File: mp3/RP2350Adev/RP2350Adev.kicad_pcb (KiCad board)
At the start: 2 copper layers, 30.9 x 51.8 mm, 44 parts, among them J1 USB4105-GF-A, J2 LEFT, J4 RIGHT, U1 W25Q32JV, U2 RP2350A, U3 MCP1702T-3302E_CB, X1 IQXO-791

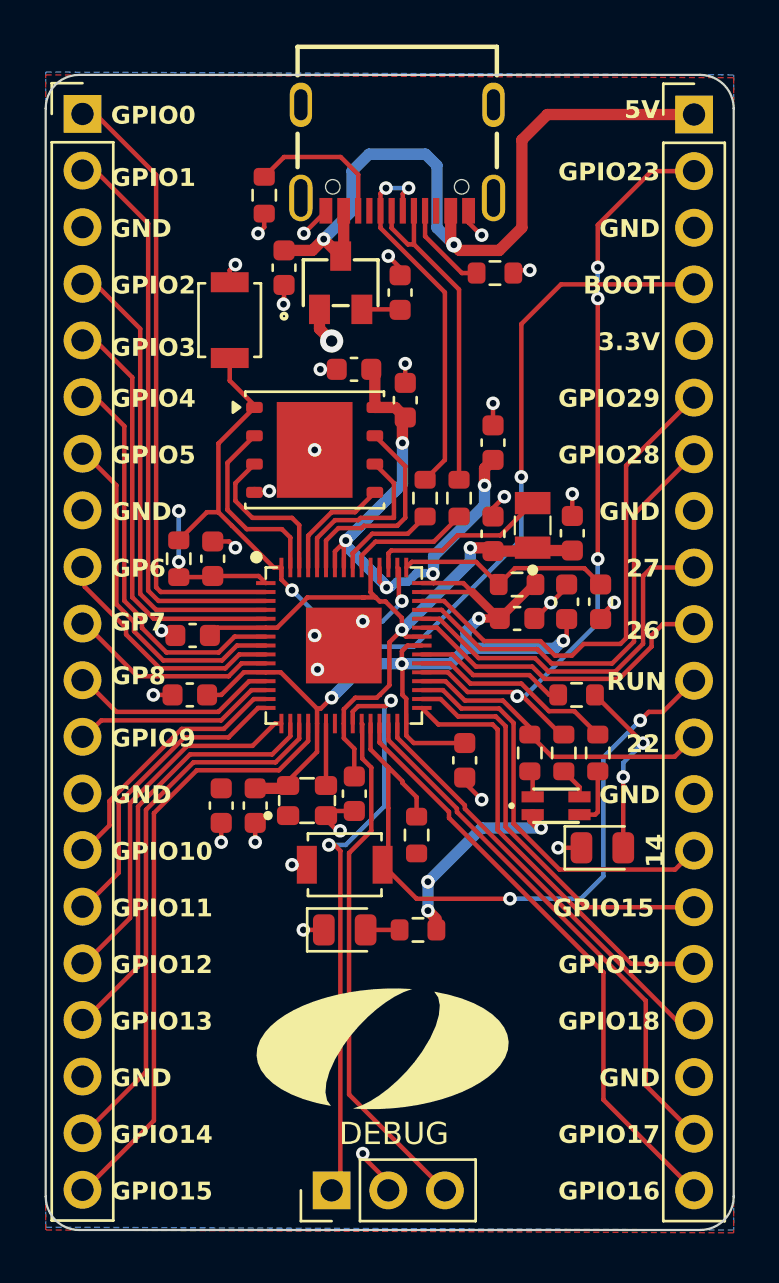
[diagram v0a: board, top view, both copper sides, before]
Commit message: Update board sizing to be 50x32mm
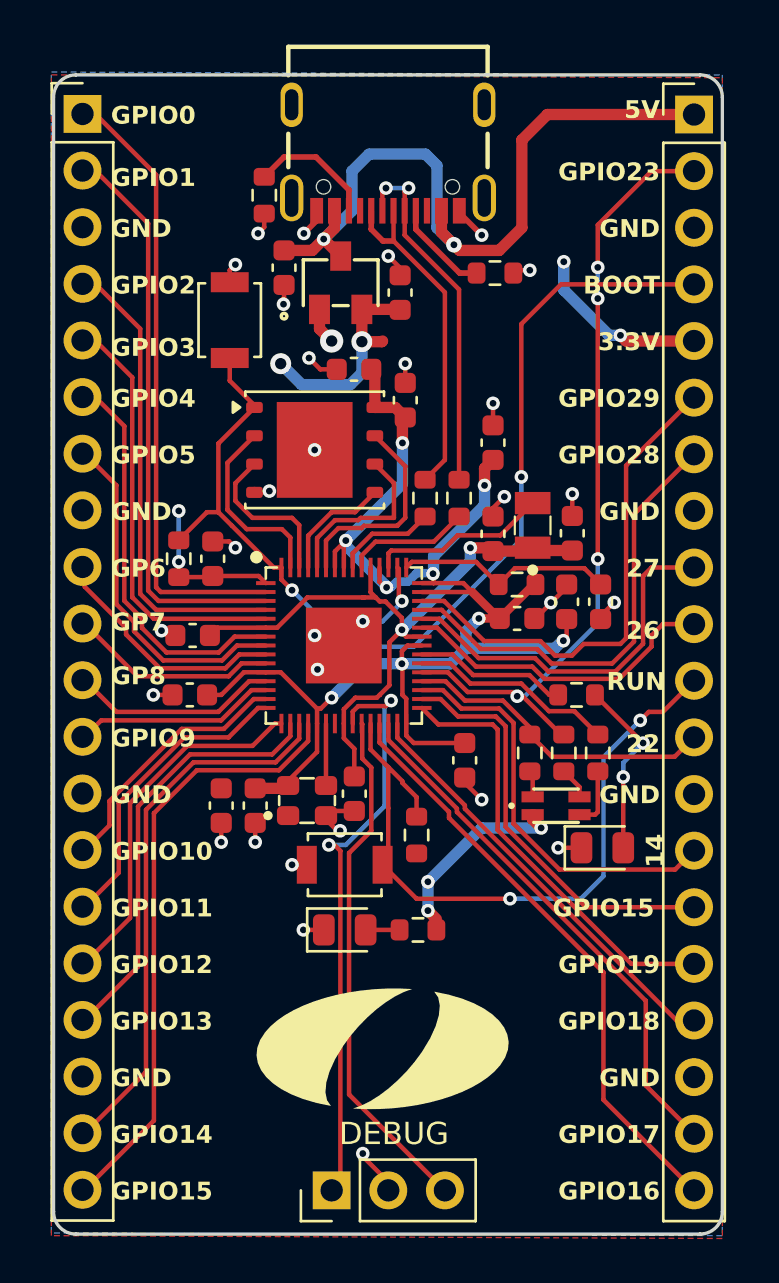
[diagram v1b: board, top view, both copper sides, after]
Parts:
- moved J1 0.41 mm to (42.7, 24.2)
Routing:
- net +3V3: track 87.6 -> 103.7 mm, vias 14 -> 18
- net Net-(J1-D+-PadA6): track 16.9 -> 15.4 mm, vias 2 -> 0
- net Net-(J1-D--PadA7): track 15.0 -> 16.3 mm, vias 0 -> 2
- net Net-(J1-CC1): track 4.14 -> 5.03 mm
- net Net-(J1-CC2): track 6.54 -> 5.72 mm
- net GND: track 42.6 -> 43.3 mm
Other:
- board size 30.9 x 51.8 mm -> 30 x 52 mm

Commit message: Add mounting holes
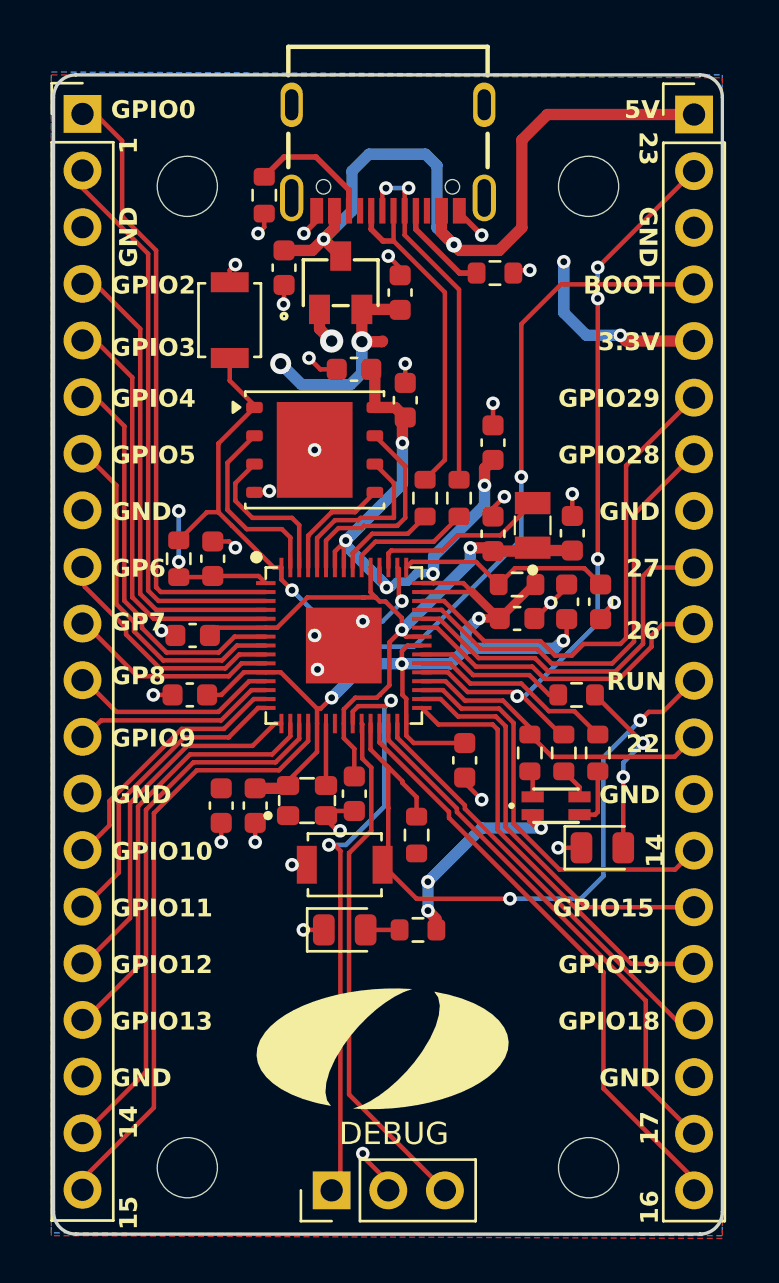
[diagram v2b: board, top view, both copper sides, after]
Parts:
- added REF**: MountingHole_2.7mm_M2.5_DIN965, MountingHole:MountingHole_2.7mm_M2.5_DIN965, F.Cu at (33.7, 27.9)
- added REF**: MountingHole_2.7mm_M2.5_DIN965, MountingHole:MountingHole_2.7mm_M2.5_DIN965, F.Cu at (51.7, 71.9)
- added REF**: MountingHole_2.7mm_M2.5_DIN965, MountingHole:MountingHole_2.7mm_M2.5_DIN965, F.Cu at (51.7, 27.9)
- added REF**: MountingHole_2.7mm_M2.5_DIN965, MountingHole:MountingHole_2.7mm_M2.5_DIN965, F.Cu at (33.7, 71.9)
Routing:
- net /GPIO23: track 35.9 -> 34.8 mm
- net +3V3: track 103.7 -> 104.3 mm
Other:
- board text added: "1"
- board text added: "15"
- board text added: "16"
- board text added: "17"
- board text added: "23"
- board text removed: "GPIO1"
- board text removed: "GPIO14"
- board text removed: "GPIO16"
- board text removed: "GPIO17"
- board text removed: "GPIO23"

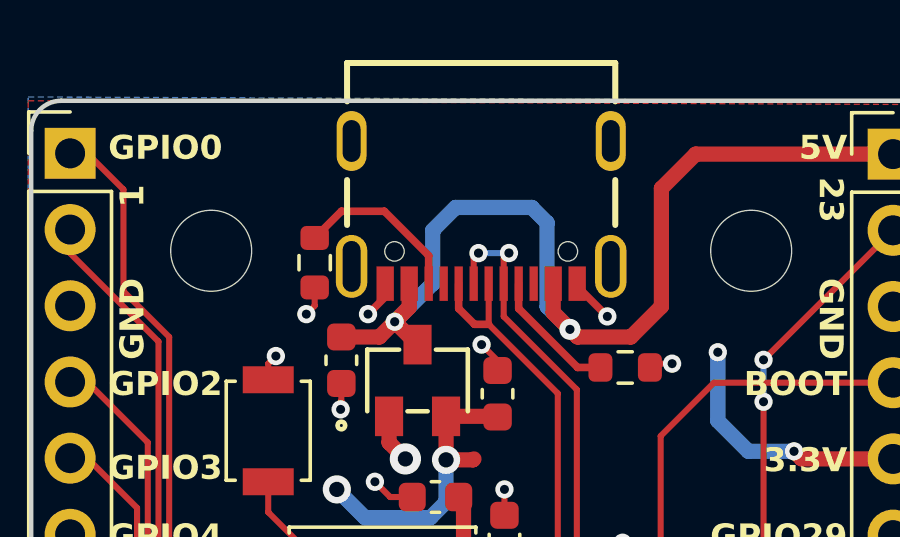
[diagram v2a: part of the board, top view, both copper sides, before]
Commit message: Update mounting holes for DRC
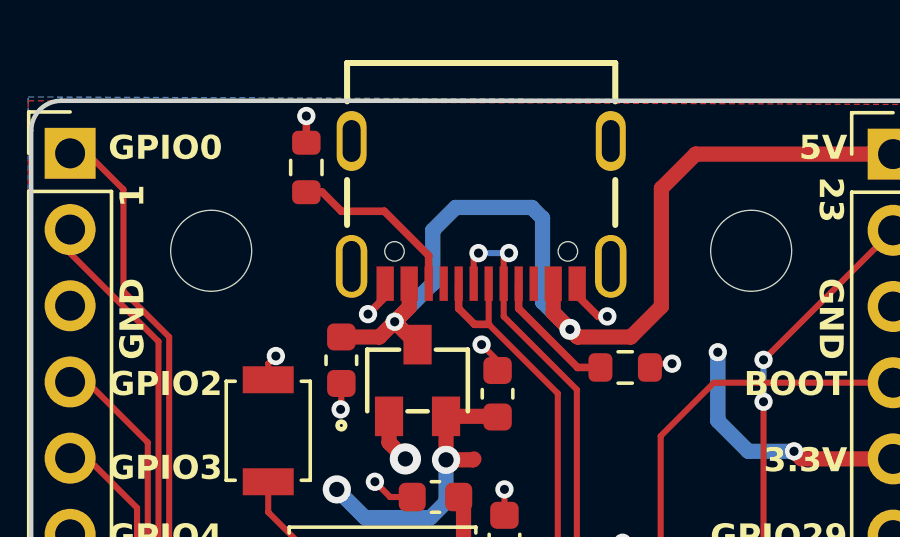
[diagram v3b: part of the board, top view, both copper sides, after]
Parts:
- moved R3 3.19 mm to (36.8, 25.1), turned to 90 degrees
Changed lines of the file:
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@@
 	(footprint "Resistor_SMD:R_0603_1608Metric"
 		(layer "F.Cu")
-		(at 37.108 28.258 -90)
+		(at 36.83 25.083 90)
 		(descr "Resistor SMD 0603 (1608 Metric), square (rectangular) end terminal, IPC-7351 nominal, (Body size source: IPC-SM-782 page 72, https://www.pcb-3d.com/wordpress/wp-content/uploads/ipc-sm-782a_amendment_1_and_2.pdf), generated with kicad-footprint-generator")
 		(tags "resistor")
@@
 		(attr smd)
 		(fp_line
-			(start -0.237258 0.5225)
-			(end 0.237258 0.5225)
+			(start -0.237258 -0.5225)
+			(end 0.237258 -0.5225)
 			(stroke
 				(width 0.12)
@@
 		)
 		(fp_line
-			(start -0.237258 -0.5225)
-			(end 0.237258 -0.5225)
+			(start -0.237258 0.5225)
+			(end 0.237258 0.5225)
 			(stroke
 				(width 0.12)
@@
 		)
 		(pad "1" smd roundrect
-			(at -0.825 0 270)
+			(at -0.825 0 90)
 			(size 0.8 0.95)
 			(layers "F.Cu" "F.Mask" "F.Paste")
@@
 		)
 		(pad "2" smd roundrect
-			(at 0.825 0 270)
+			(at 0.825 0 90)
 			(size 0.8 0.95)
 			(layers "F.Cu" "F.Mask" "F.Paste")
@@
 	)
 	(segment
+		(start 45.858 29.348)
+		(end 46.5582 30.0482)
+		(width 0.254)
+		(layer "F.Cu")
+		(net 2)
+	)
+	(segment
 		(start 39.878 56.087)
 		(end 39.544 56.087)
@@
 	)
 	(segment
+		(start 46.5582 30.0482)
+		(end 46.863 30.0482)
+		(width 0.254)
+		(layer "F.Cu")
+		(net 2)
+	)
+	(segment
 		(start 41.148 55.88)
 		(end 40.085 55.88)
@@
 	)
 	(segment
-		(start 36.83 29.972)
-		(end 37.108 29.694)
-		(width 0.2032)
-		(layer "F.Cu")
-		(net 2)
-	)
-	(segment
 		(start 46.101 54.382)
 		(end 46.101 54.61)
@@
 	)
 	(segment
-		(start 45.858 29.0432)
-		(end 46.863 30.0482)
-		(width 0.254)
-		(layer "F.Cu")
-		(net 2)
-	)
-	(segment
 		(start 41.529 71.247)
 		(end 41.529 71.374)
@@
 	)
 	(segment
+		(start 36.83 24.258)
+		(end 36.83 23.368)
+		(width 0.254)
+		(layer "F.Cu")
+		(net 2)
+	)
+	(segment
 		(start 40.678 48.458)
 		(end 39.822 48.458)
@@
 	)
 	(segment
+		(start 45.858 28.956)
+		(end 45.858 29.348)
+		(width 0.254)
+		(layer "F.Cu")
+		(net 2)
+	)
+	(segment
 		(start 47.371 42.291)
 		(end 47.879 41.783)
@@
 	)
 	(segment
-		(start 37.108 29.694)
-		(end 37.108 29.083)
-		(width 0.2032)
-		(layer "F.Cu")
-		(net 2)
-	)
-	(segment
 		(start 37.211 41.529)
 		(end 37.152 41.588)
@@
 	)
 	(segment
-		(start 45.858 28.956)
-		(end 45.858 29.0432)
-		(width 0.254)
-		(layer "F.Cu")
-		(net 2)
-	)
-	(segment
 		(start 49.276 47.244)
 		(end 49.2252 47.244)
@@
 	)
 	(via
-		(at 36.83 29.972)
-		(size 0.6096)
-		(drill 0.3)
-		(layers "F.Cu" "B.Cu")
-		(net 2)
-	)
-	(via
 		(at 40.132 34.798)
 		(size 1.0414)
@@
 	)
 	(via
+		(at 36.83 23.368)
+		(size 0.6096)
+		(drill 0.3048)
+		(layers "F.Cu" "B.Cu")
+		(net 2)
+	)
+	(via
 		(at 35.179 57.277)
 		(size 0.6096)
@@
 	)
 	(segment
-		(start 44.855 29.718)
+		(start 44.704 29.567)
 		(end 45.617 30.48)
 		(width 0.508)
@@
 	)
 	(segment
-		(start 39.775 30.226)
-		(end 41.045 28.956)
+		(start 44.704 26.773)
+		(end 44.704 29.567)
 		(width 0.508)
 		(layer "B.Cu")
@@
 	)
 	(segment
-		(start 44.347 26.416)
-		(end 44.855 26.924)
+		(start 39.775 30.226)
+		(end 41.045 28.956)
 		(width 0.508)
 		(layer "B.Cu")
@@
 	)
 	(segment
-		(start 44.855 26.924)
-		(end 44.855 29.718)
+		(start 41.045 27.178)
+		(end 41.807 26.416)
 		(width 0.508)
 		(layer "B.Cu")
@@
 	)
 	(segment
-		(start 41.045 27.178)
-		(end 41.807 26.416)
+		(start 41.045 28.956)
+		(end 41.045 27.178)
 		(width 0.508)
 		(layer "B.Cu")
@@
 	)
 	(segment
-		(start 41.807 26.416)
-		(end 44.347 26.416)
+		(start 44.347 26.416)
+		(end 44.704 26.773)
 		(width 0.508)
 		(layer "B.Cu")
@@
 	)
 	(segment
-		(start 41.045 28.956)
-		(end 41.045 27.178)
+		(start 41.807 26.416)
+		(end 44.347 26.416)
 		(width 0.508)
 		(layer "B.Cu")
@@
 	)
 	(segment
-		(start 37.108 27.433)
+		(start 37.363 25.908)
 		(end 37.998 26.543)
 		(width 0.254)
@@
 		(width 0.254)
 		(layer "F.Cu")
+		(net 15)
+	)
+	(segment
+		(start 36.83 25.908)
+		(end 37.363 25.908)
+		(width 0.254)
+		(layer "F.Cu")

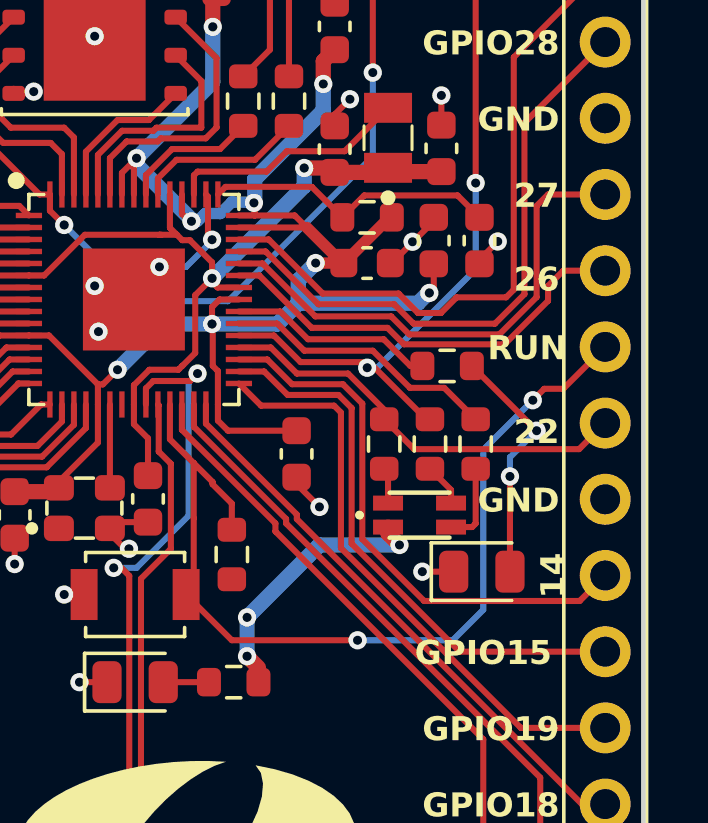
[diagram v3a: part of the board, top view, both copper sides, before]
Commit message: Nudge bottom layer traces
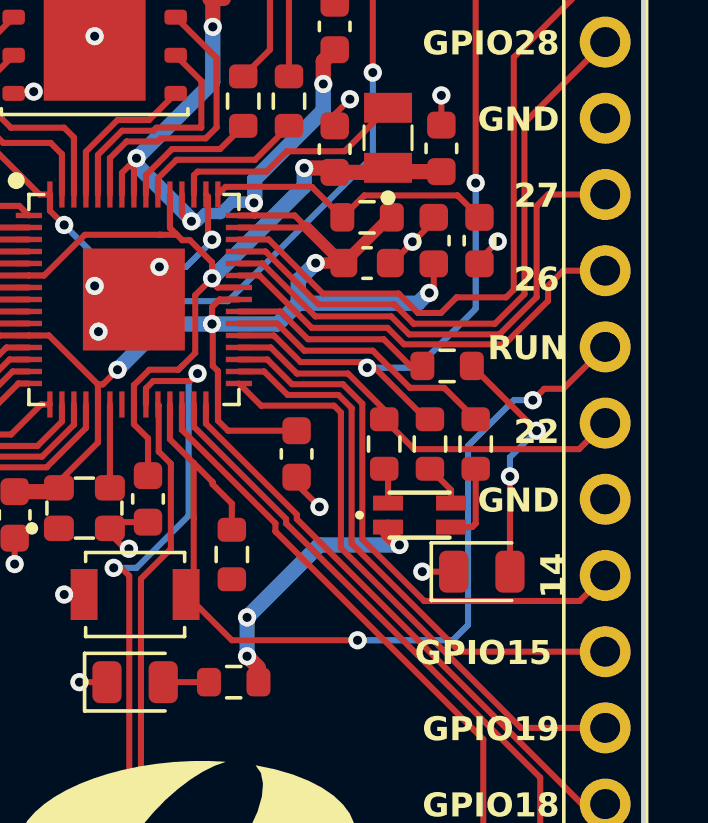
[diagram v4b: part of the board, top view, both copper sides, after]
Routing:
- net /GPIO23: track 34.8 -> 35.5 mm
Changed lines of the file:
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@@
-	)
-	(segment
-		(start 48.454027 50.732973)
-		(end 48.788348 50.732973)
-		(width 0.2032)
-		(layer "B.Cu")
-		(net 38)
 	)
 	(segment
@@
 	)
 	(segment
-		(start 48.788348 50.732973)
-		(end 52.07 47.451321)
+		(start 50.105027 50.732973)
+		(end 52.07 48.768)
 		(width 0.2032)
 		(layer "B.Cu")
@@
 	)
 	(segment
-		(start 52.07 47.451321)
+		(start 48.454027 50.732973)
+		(end 50.105027 50.732973)
+		(width 0.2032)
+		(layer "B.Cu")
+		(net 38)
+	)
+	(segment
+		(start 52.07 48.768)
 		(end 52.07 44.577)
 		(width 0.2032)
@@
 	)
 	(segment
-		(start 52.324 53.467)
-		(end 52.324 58.801)
-		(width 0.2032)
-		(layer "B.Cu")
-		(net 44)
-	)
-	(segment
-		(start 52.324 58.801)
+		(start 51.308 59.817)
+		(end 48.133 59.817)
+		(width 0.2032)
+		(layer "B.Cu")
+		(net 44)
+	)
+	(segment
+		(start 51.816 59.309)
 		(end 51.308 59.817)
 		(width 0.2032)
@@
 	)
 	(segment
+		(start 51.816 53.34)
+		(end 51.816 59.309)
+		(width 0.2032)
+		(layer "B.Cu")
+		(net 44)
+	)
+	(segment
+		(start 53.34 51.816)
+		(end 51.816 53.34)
+		(width 0.2032)
+		(layer "B.Cu")
+		(net 44)
+	)
+	(segment
 		(start 53.975 51.816)
-		(end 52.324 53.467)
-		(width 0.2032)
-		(layer "B.Cu")
-		(net 44)
-	)
-	(segment
-		(start 51.308 59.817)
-		(end 48.133 59.817)
-		(width 0.2032)
-		(layer "B.Cu")
+		(end 53.34 51.816)
+		(width 0.2032)
+		(layer "B.Cu")

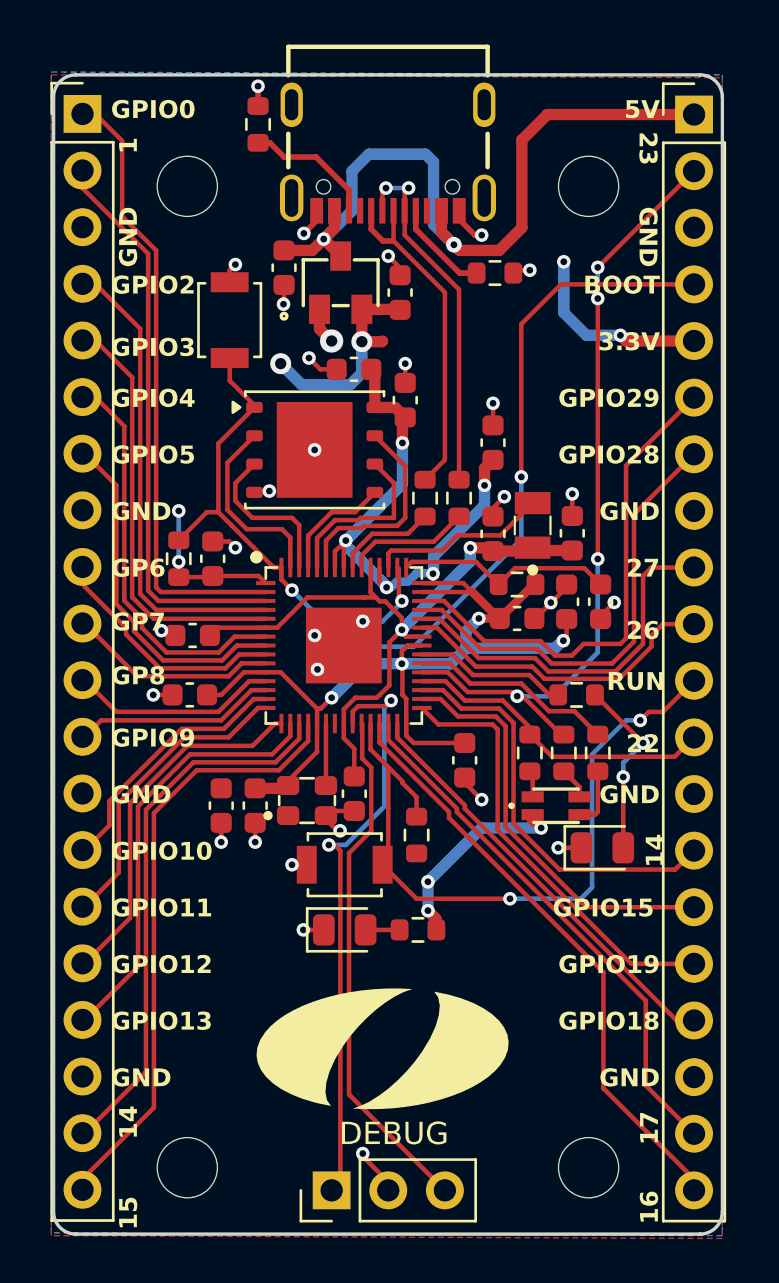
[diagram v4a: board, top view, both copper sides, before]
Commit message: Remove Custom Rules from PCBWay
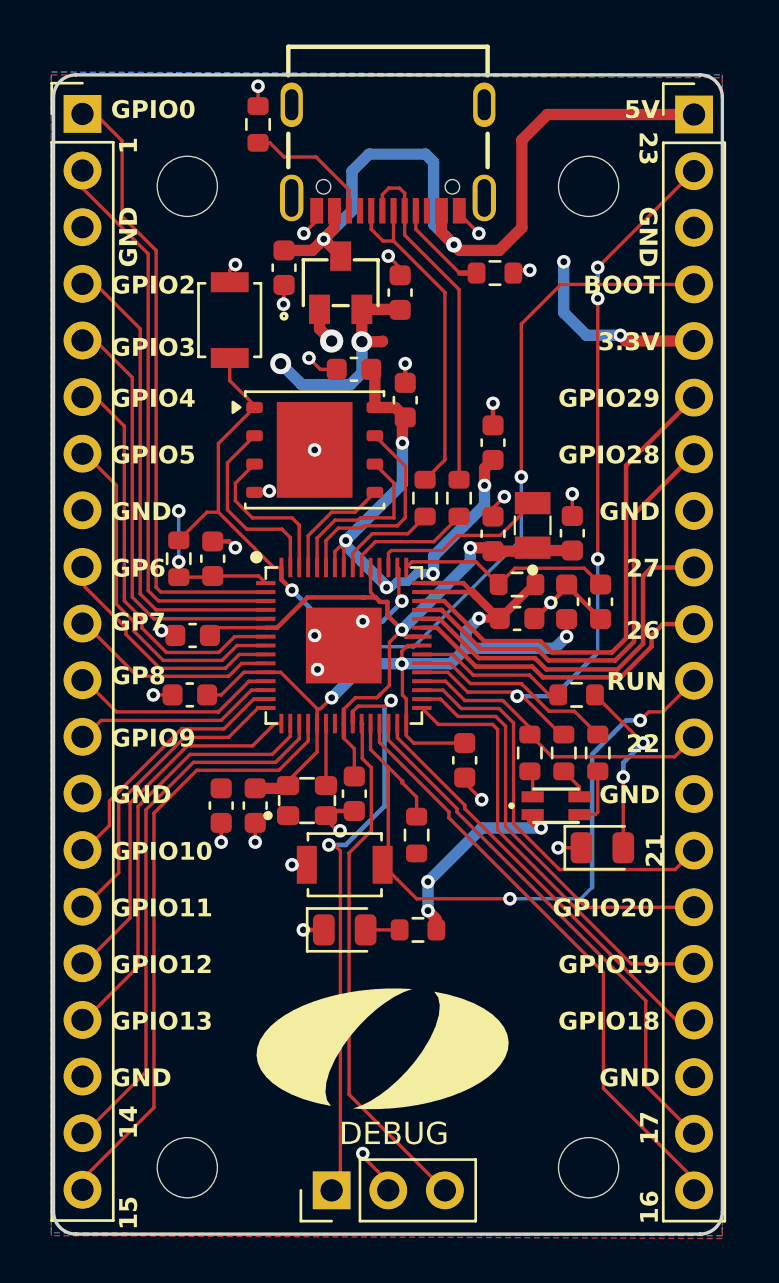
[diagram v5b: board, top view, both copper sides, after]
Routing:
- net GND: track 43.4 -> 44.8 mm, vias 32 -> 31
- net Net-(J1-D--PadA7): track 16.3 -> 15.8 mm, vias 2 -> 0
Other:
- board text added: "21"
- board text added: "GPIO20"
- board text removed: "GPIO15"
